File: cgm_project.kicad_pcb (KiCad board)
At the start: 2 copper layers, 50 x 70 mm, 34 parts, among them J1 JST BATT CONNECTOR, J2 USB_C_Receptacle_USB2.0_16P, J3 Conn_01x02, J4 Conn_01x02_MountingPin, Q1 AO3400, SW1 SW_SPDT, U1 TP4056-42-ESOP8, U2 AP2112K-3.3, U3 ESP32-C3-WROOM-02, U5 OPA380

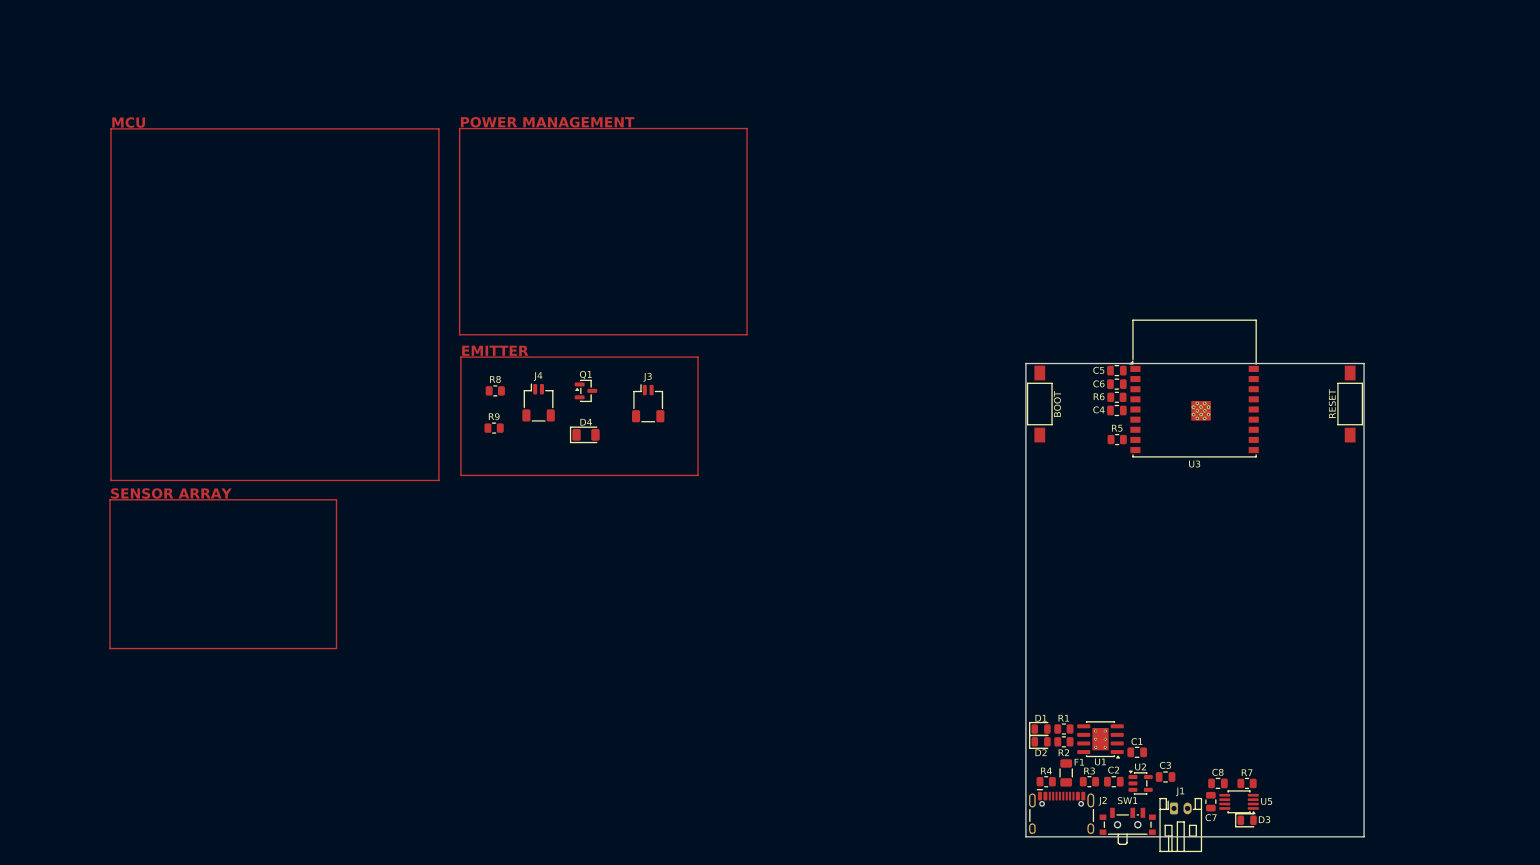
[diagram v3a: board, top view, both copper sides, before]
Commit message: chore: finalize placement for emitter connector, current switch, limiter, and gate pulldown
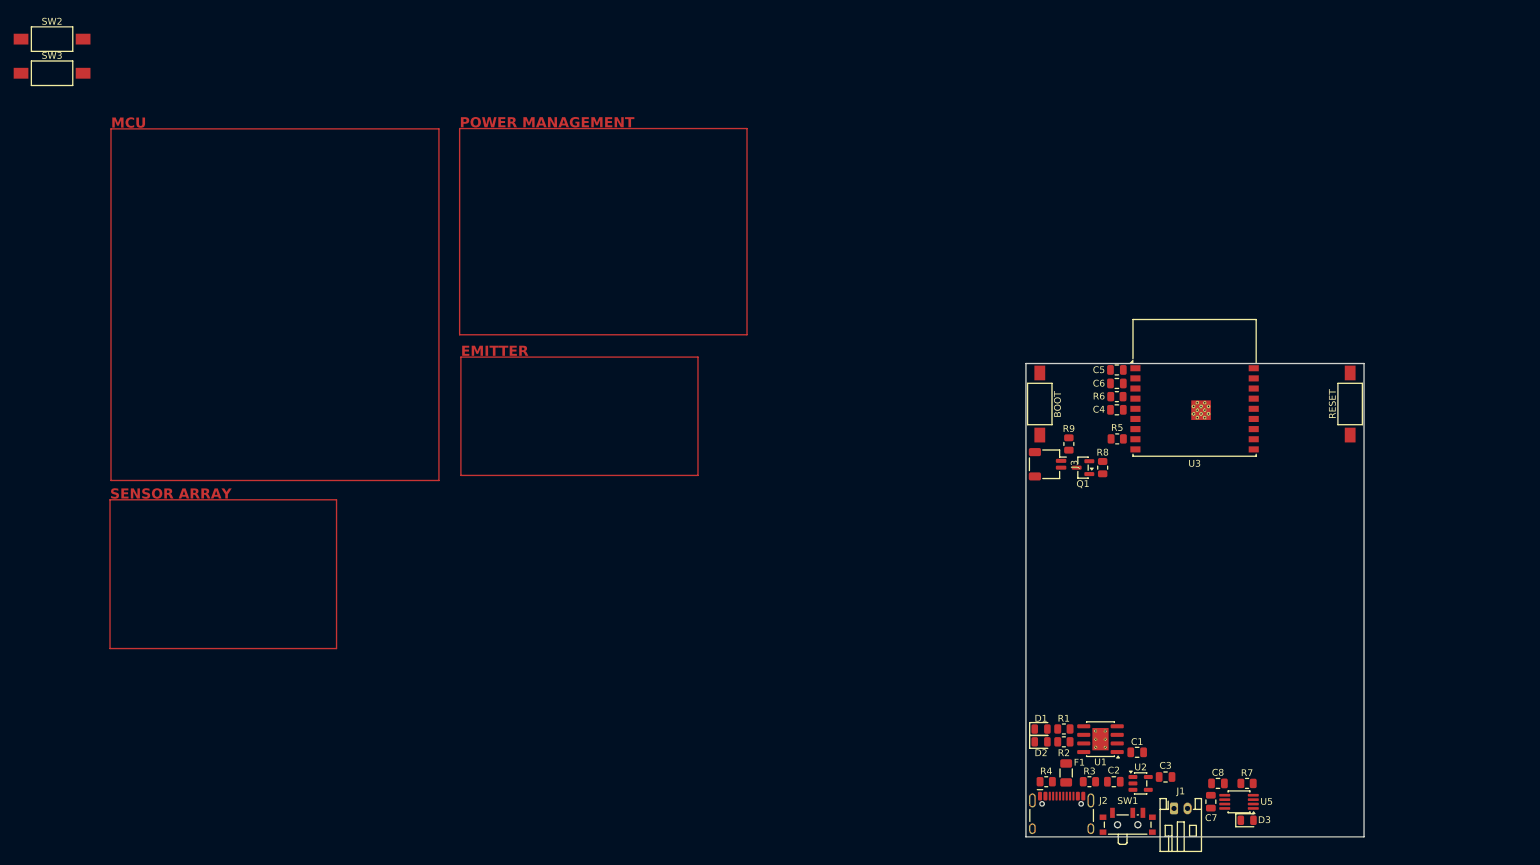
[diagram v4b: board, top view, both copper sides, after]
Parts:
- removed D4: IR26-21C_L110_TR8, LED_SMD:LED_1206_3216Metric
- removed J4: Conn_01x02_MountingPin, Connector_JST:JST_SH_SM02B-SRSS-TB_1x02-1MP_P1.00mm_Horizontal
- added SW2: BOOT, Button_Switch_SMD:SW_SPST_FSMSM, F.Cu at (5.97, 2.02)
- added SW3: RESET, Button_Switch_SMD:SW_SPST_FSMSM, F.Cu at (5.97, 7.08)
- J3: value Conn_01x02 -> Conn_01x02_MountingPin
- moved R8 90.5 mm to (161.3, 65.4), turned to 90 degrees
- moved R9 85.0 mm to (156.3, 61.9), turned to -90 degrees
- moved Q1 74.4 mm to (158.4, 65.4), turned to 180 degrees
- moved J3 59.7 mm to (153.2, 64.9), turned to -90 degrees
- moved C4 0.10 mm to (163.4, 56.9)
- moved R5 0.10 mm to (163.5, 61.1)
- moved R6 0.10 mm to (163.4, 54.9)
- moved C5 0.10 mm to (163.4, 51.0)
- moved C6 0.10 mm to (163.4, 53.0)
- moved U3 0.10 mm to (174.9, 56.7)
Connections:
- J3 pad MP: (no net) -> GND
- Q1 pad 3: Net-(J4-Pin_2) -> Net-(J3-Pin_2)
- R9 pad 2: Net-(J4-Pin_1) -> Net-(J3-Pin_1)

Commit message: chore: switched to a double sided design - changed BOOT and RST to a more compact footpritn - moved all connectors and switches to front of board
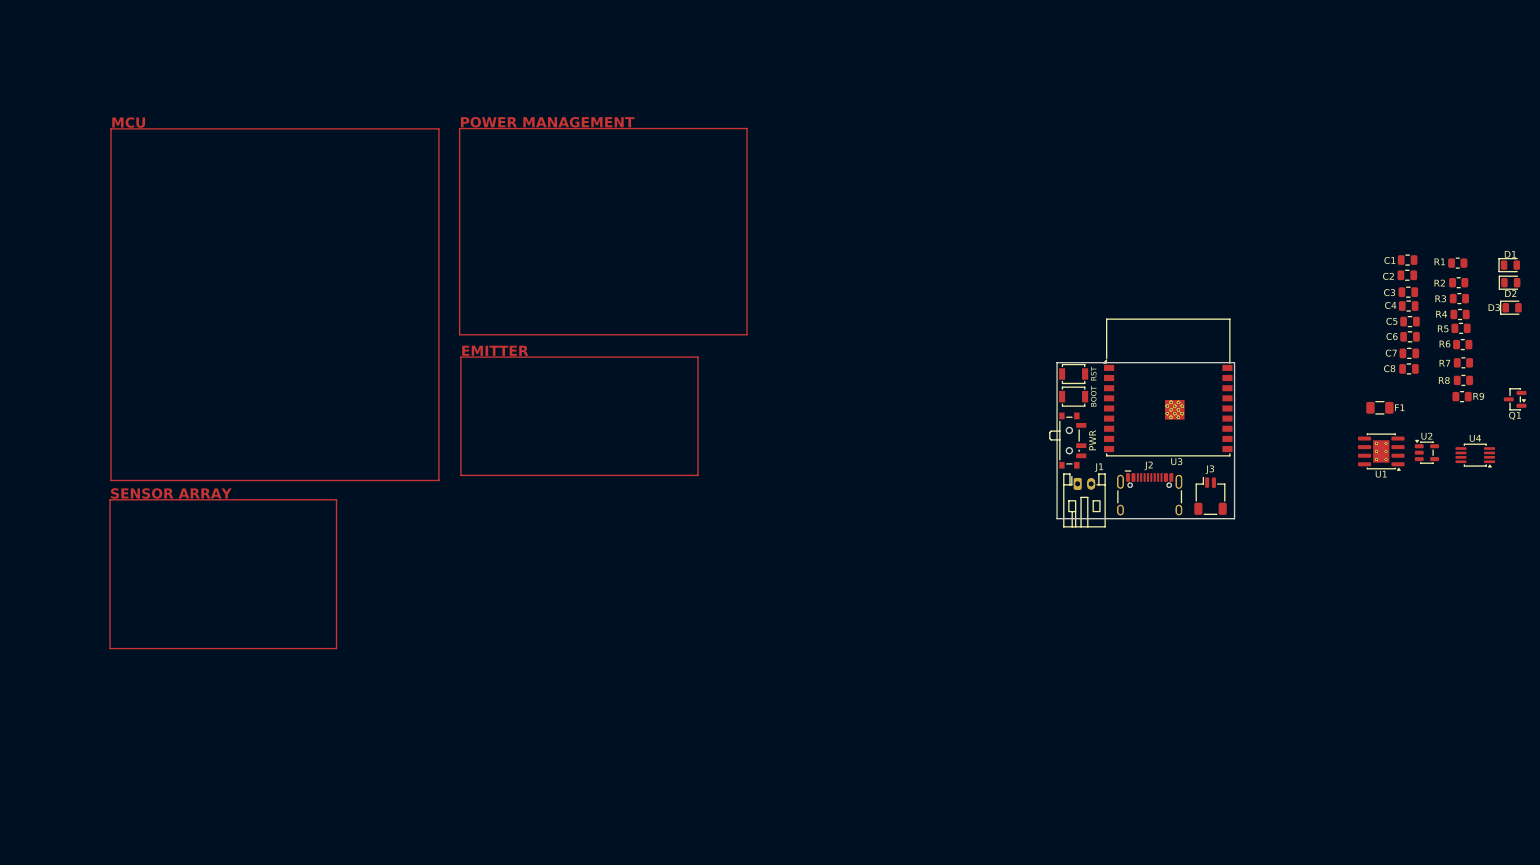
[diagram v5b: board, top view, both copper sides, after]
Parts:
- removed the BOOT at (152.1, 56.0)
- removed RESET, SW3: RESET, Button_Switch_SMD:SW_SPST_FSMSM
- removed SW2: BOOT, Button_Switch_SMD:SW_SPST_FSMSM
- added BOOT: BOOT, Button_Switch_SMD:SW_SPST_B3U-1000P, F.Cu at (157.1, 54.9)
- added RST: RESET, Button_Switch_SMD:SW_SPST_B3U-1000P, F.Cu at (157.1, 51.5)
- moved D1 97.6 mm to (221.7, 35.5)
- moved D2 97.1 mm to (221.7, 38.0)
- moved R4 92.3 mm to (214.2, 42.8), turned to 0 degrees
- moved R1 90.2 mm to (213.9, 35.1)
- moved R3 90.0 mm to (214.1, 40.4), turned to 0 degrees
- moved R2 89.6 mm to (214.0, 38.0)
- moved C2 86.6 mm to (206.4, 37.0), turned to 180 degrees
- moved D3 85.3 mm to (221.9, 41.8)
- moved C1 83.1 mm to (206.4, 34.7), turned to 0 degrees
- moved C3 80.2 mm to (206.6, 39.5), turned to 180 degrees
- moved C7 72.5 mm to (206.7, 48.5), turned to 180 degrees
- moved F1 71.2 mm to (202.3, 56.5), turned to 180 degrees
- moved R7 69.9 mm to (214.7, 49.9)
- moved C8 67.5 mm to (206.7, 50.8)
- moved Q1 64.7 mm to (222.3, 55.3)
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- renumbered SW1 to PWR, U5 to U4
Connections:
- Q1 pad 3: Net-(J3-Pin_2) -> Net-(J4-Pin_2)
- R9 pad 2: Net-(J3-Pin_1) -> Net-(J4-Pin_1)
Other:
- board size 50 x 70 mm -> 26.2 x 23.1 mm

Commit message: chore: placement of photodiode sensor array on bottom of PCB
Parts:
- C7, C8, D3, R7, U4: moved to B.Cu
- moved D3 57.7 mm to (167.7, 61.4), turned to 180 degrees
- moved R7 51.5 mm to (163.7, 57.2), turned to -90 degrees
- moved U4 50.4 mm to (166.4, 57.2), turned to 90 degrees
- moved C8 45.4 mm to (161.8, 57.2), turned to -90 degrees
- moved C7 38.2 mm to (168.9, 53.8), turned to -90 degrees

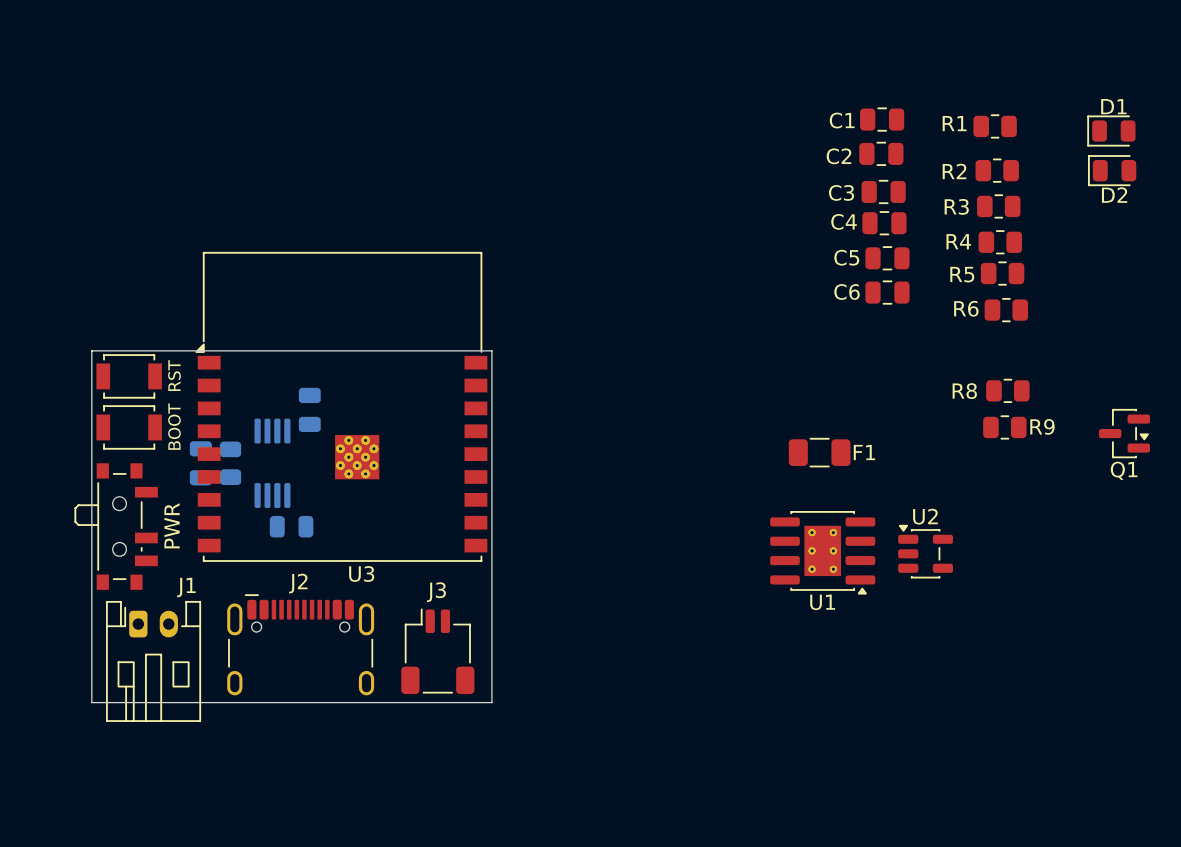
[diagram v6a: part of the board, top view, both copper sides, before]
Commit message: chore: placement of charger, LDO, fuse, and passives on back of PCB
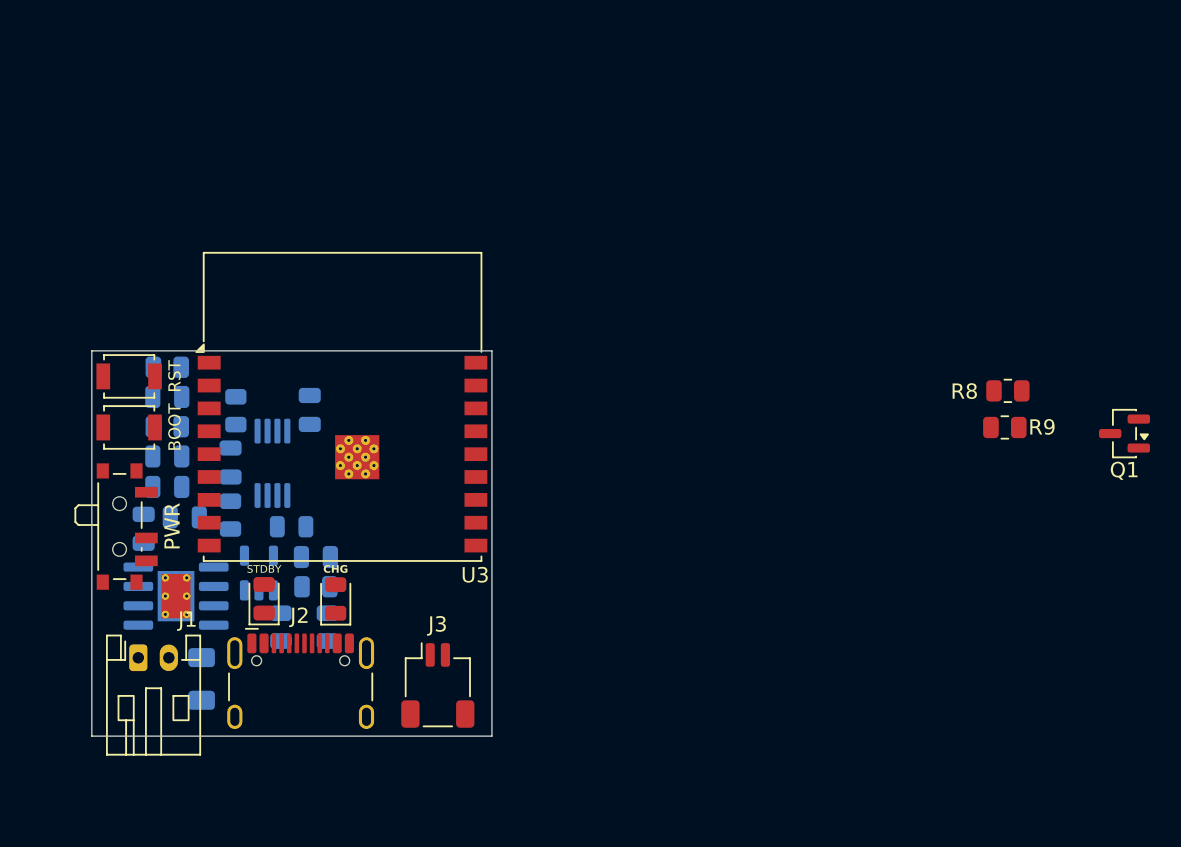
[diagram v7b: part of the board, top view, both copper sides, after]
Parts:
- C1, C2, C3, C4, C5, C6, F1, R1, R2, R3, R4, R5, R6, U1, U2: moved to B.Cu
- moved STDBY 63.6 mm to (165.9, 66.1), turned to 90 degrees
- moved CHG 58.3 mm to (170.6, 66.2), turned to 90 degrees
- moved R6 55.6 mm to (159.6, 54.9)
- moved C1 55.4 mm to (158.0, 61.5), turned to 90 degrees
- moved R5 55.1 mm to (159.6, 51.0), turned to 180 degrees
- moved R2 55.1 mm to (163.7, 60.6), turned to 90 degrees
- moved R3 54.6 mm to (167.0, 68.0), turned to 90 degrees
- moved R1 53.8 mm to (169.3, 65.3), turned to 180 degrees
- moved C2 51.5 mm to (160.7, 60.8), turned to 0 degrees
- moved R4 50.9 mm to (170.1, 68.0), turned to 90 degrees
- moved C5 49.0 mm to (159.6, 56.8)
- moved C6 48.9 mm to (159.6, 58.8)
- moved C4 48.4 mm to (159.6, 52.9), turned to 0 degrees
- moved C3 44.3 mm to (169.3, 63.4), turned to 0 degrees
- moved U2 43.8 mm to (165.6, 64.5), turned to 90 degrees
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- renumbered D2 to CHG, D1 to STDBY
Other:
- board size 26.2 x 23.1 mm -> 26.2 x 25.3 mm

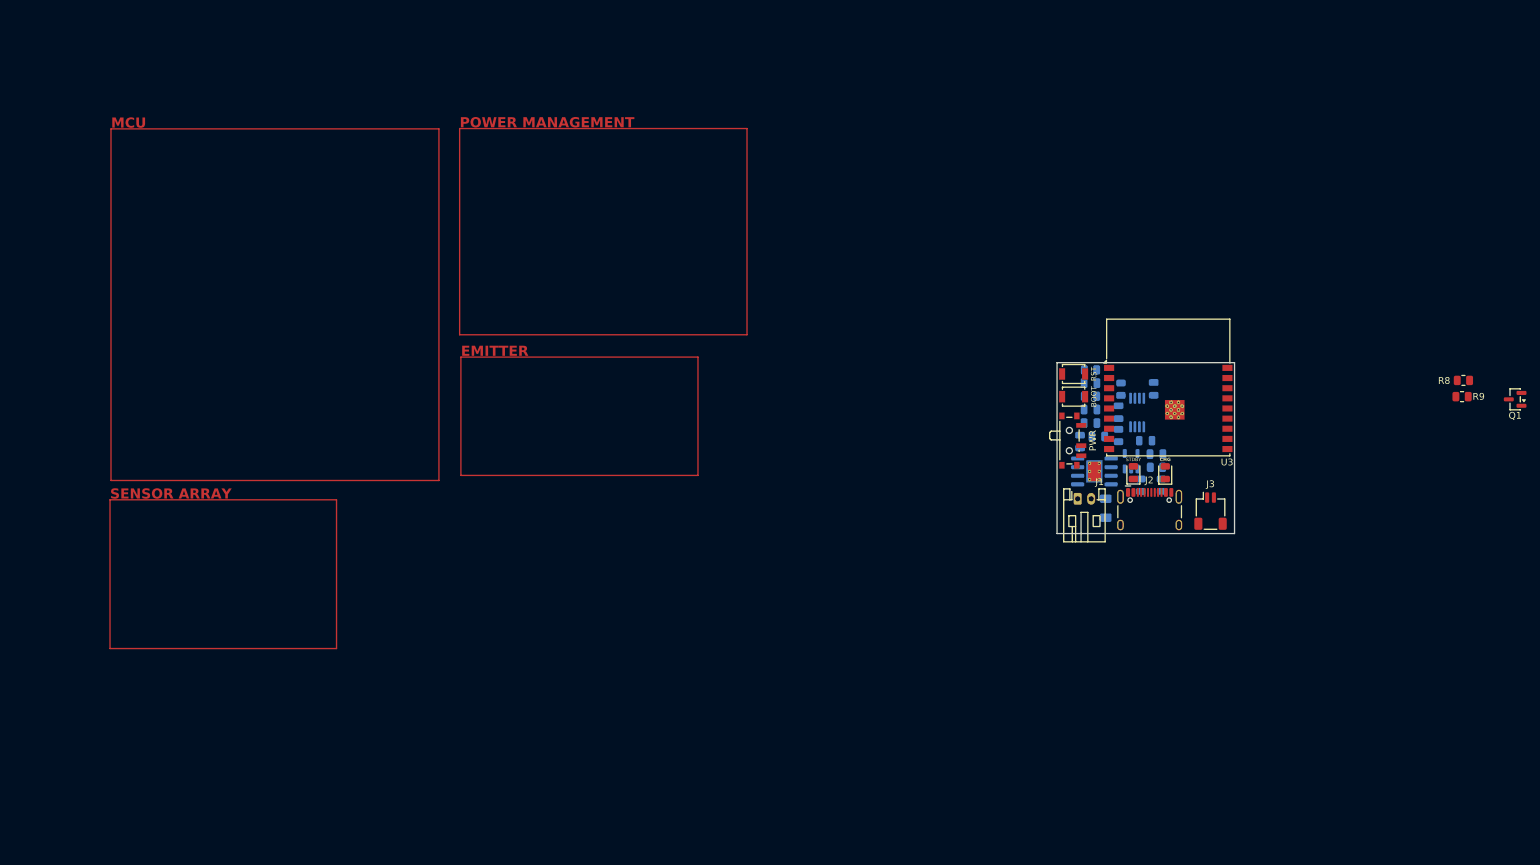
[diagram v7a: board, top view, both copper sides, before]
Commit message: chore: finalize double-sided PCB floorplan - lock footprint positions for routing - position D3 for optimal finger placement - stack U4 analog island directly beaneath U3 to minimize noise on analog signals - esablish decoupling wall (C4, C5, C6) under ESP32 to minimize impedence - verify z-axis clearance bettwen U1 and U2 surface mount packages and J1 and J2 through-hole pins
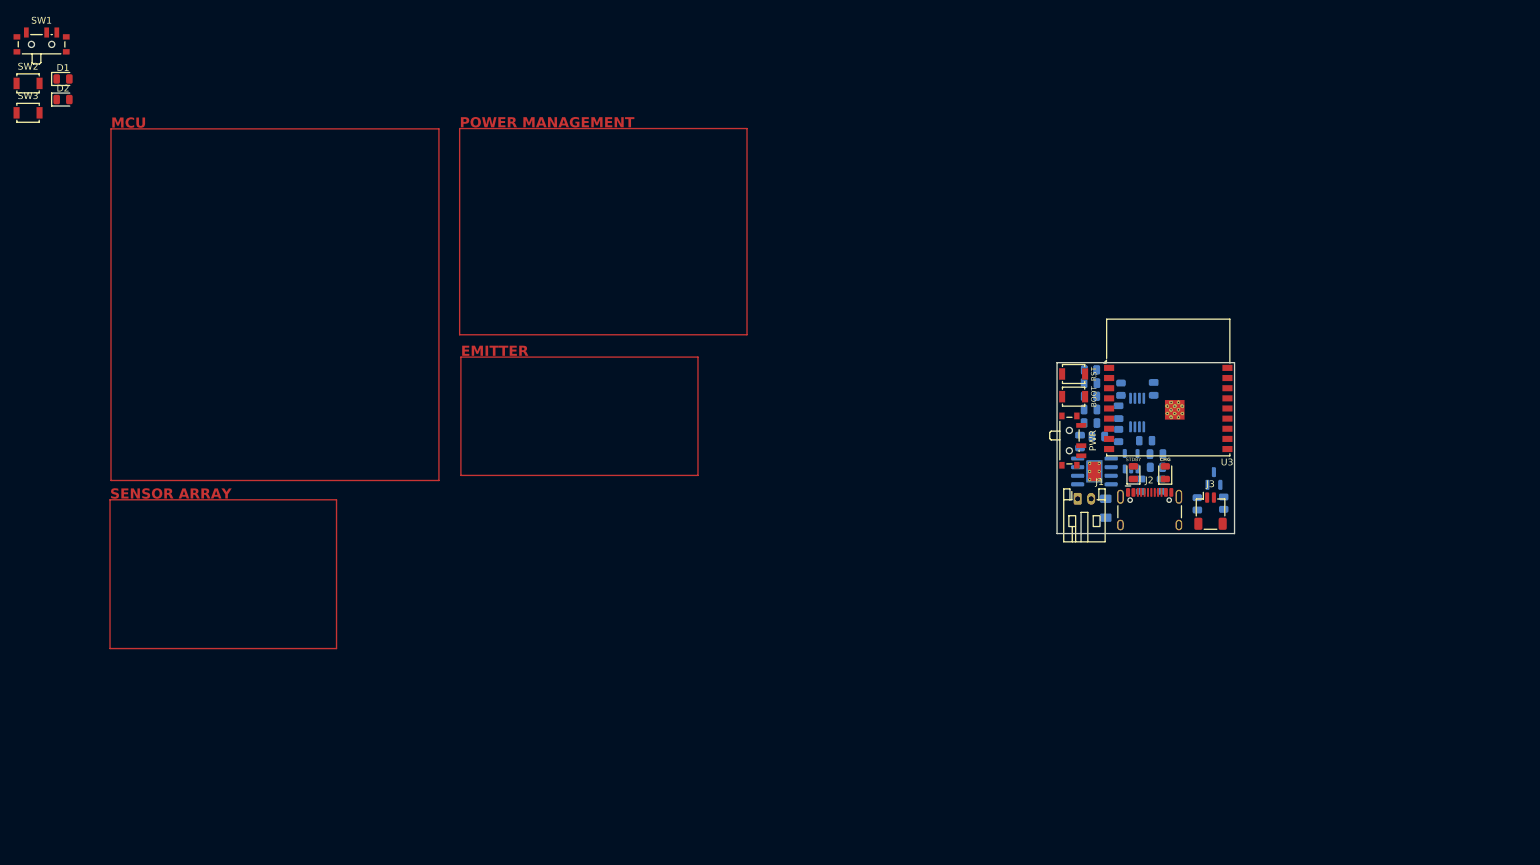
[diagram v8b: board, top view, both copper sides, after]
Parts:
- added D1: GREEN LED, LED_SMD:LED_0805_2012Metric, F.Cu at (7.59, 7.92)
- added D2: RED LED, LED_SMD:LED_0805_2012Metric, F.Cu at (7.59, 11.0)
- added SW1: SW_SPDT, Button_Switch_SMD:SW_SPDT_PCM12, F.Cu at (4.42, 2.48)
- added SW2: BOOT, Button_Switch_SMD:SW_SPST_B3U-1000P, F.Cu at (2.42, 8.57)
- added SW3: RESET, Button_Switch_SMD:SW_SPST_B3U-1000P, F.Cu at (2.42, 12.9)
- Q1, R8, R9: moved to B.Cu
- moved Q1 46.1 mm to (177.8, 67.0), turned to 90 degrees
- moved R9 42.2 mm to (175.3, 70.8), turned to 90 degrees
- moved R8 39.8 mm to (179.2, 70.7), turned to -90 degrees
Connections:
- Q1 pad 3: Net-(J4-Pin_2) -> Net-(J3-Pin_2)
- R9 pad 2: Net-(J4-Pin_1) -> Net-(J3-Pin_1)
